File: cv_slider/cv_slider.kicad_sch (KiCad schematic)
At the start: 11 parts, among them J1 I/O connector, U1 HT7550-1, U2 TLV6001UIDBVR

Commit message: Added LCSC part
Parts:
- U2: LCSC (none) -> C544299
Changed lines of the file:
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@@
       (effects (font (size 1.27 1.27)) (justify left) hide)
     )
-    (property "Datasheet" "" (id 3) (at 144.78 99.06 0)
+    (property "Datasheet" "https://www.ti.com/lit/ds/symlink/tlv6001.pdf" (id 3) (at 144.78 99.06 0)
       (effects (font (size 1.27 1.27)) hide)
     )
+    (property "LCSC" "C544299" (id 4) (at 144.78 104.14 0)
+      (effects (font (size 1.524 1.524)) hide)
+    )
     (pin "2")

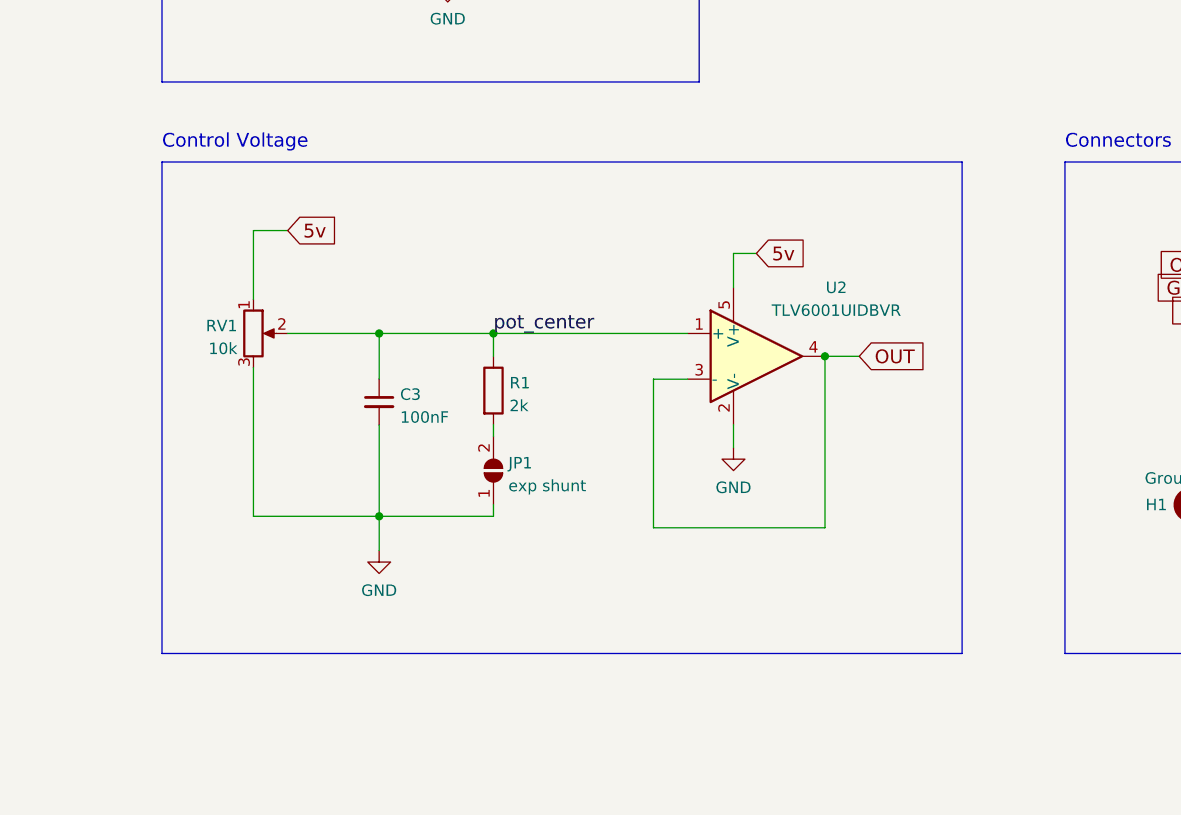
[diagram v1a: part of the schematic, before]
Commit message: Added 1k output resistor
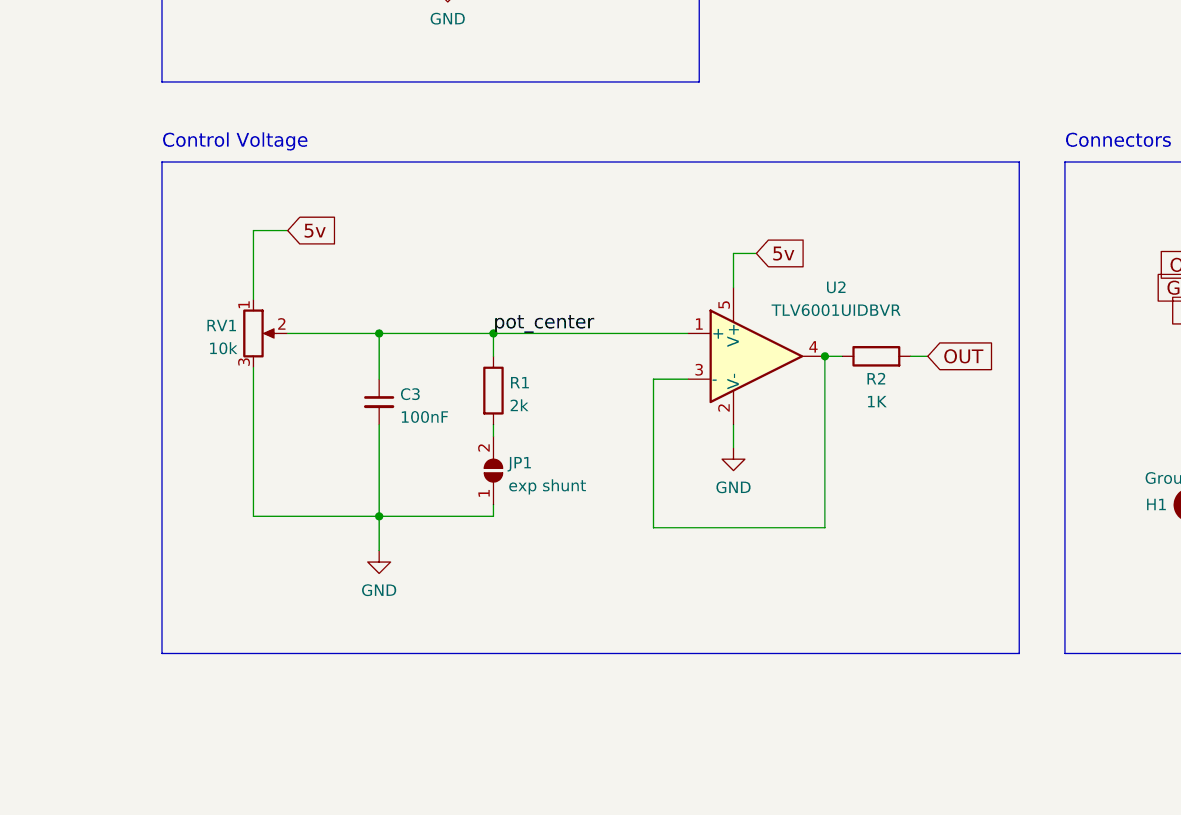
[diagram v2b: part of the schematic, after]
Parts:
- added R2: 1K, Resistor_SMD:R_0402_1005Metric, symbol Device:R
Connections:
- net OUT: now also R2.2; no longer U2.3 (-), U2.4
- new net: R2.1, U2.3 (-), U2.4
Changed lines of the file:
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@@
-    (stroke (width 0) (type default) (color 0 0 0 0))
-  )
-  (wire (pts (xy 152.4 104.14) (xy 156.21 104.14))
     (stroke (width 0) (type default) (color 0 0 0 0))
   )
@@
     (stroke (width 0) (type default) (color 0 0 0 0))
   )
-  (polyline (pts (xy 78.74 82.55) (xy 167.64 82.55))
+  (polyline (pts (xy 78.74 82.55) (xy 173.99 82.55))
     (stroke (width 0) (type default) (color 0 0 0 0))
   )
@@
     (stroke (width 0) (type default) (color 0 0 0 0))
   )
-  (polyline (pts (xy 167.64 82.55) (xy 167.64 137.16))
+  (polyline (pts (xy 173.99 82.55) (xy 173.99 137.16))
+    (stroke (width 0) (type default) (color 0 0 0 0))
+  )
+  (wire (pts (xy 161.925 104.14) (xy 163.83 104.14))
     (stroke (width 0) (type default) (color 0 0 0 0))
   )
@@
     (stroke (width 0) (type default) (color 0 0 0 0))
   )
-  (polyline (pts (xy 167.64 137.16) (xy 78.74 137.16))
+  (polyline (pts (xy 173.99 137.16) (xy 78.74 137.16))
     (stroke (width 0) (type default) (color 0 0 0 0))
   )
@@
   )
   (wire (pts (xy 142.24 96.52) (xy 142.24 92.71))
+    (stroke (width 0) (type default) (color 0 0 0 0))
+  )
+  (wire (pts (xy 152.4 104.14) (xy 154.305 104.14))
     (stroke (width 0) (type default) (color 0 0 0 0))
   )
@@
     )
   )
-  (global_label "OUT" (shape input) (at 156.21 104.14 0) (fields_autoplaced)
+  (global_label "OUT" (shape input) (at 163.83 104.14 0) (fields_autoplaced)
     (effects (font (size 1.524 1.524)) (justify left))
-    (property "Intersheet References" "${INTERSHEET_REFS}" (id 0) (at 163.3532 104.0448 0)
+    (property "Intersheet References" "${INTERSHEET_REFS}" (id 0) (at 170.9732 104.0448 0)
       (effects (font (size 1.524 1.524)) (justify left) hide)
     )
@@
     )
     (pin "1")
+  )
+  (symbol (lib_id "Device:R") (at 158.115 104.14 90) (unit 1)
+    (in_bom yes) (on_board yes)
+    (property "Reference" "R2" (id 0) (at 158.115 106.6831 90))
+    (property "Value" "1K" (id 1) (at 158.115 109.22 90))
+    (property "Footprint" "Resistor_SMD:R_0402_1005Metric" (id 2) (at 158.115 105.918 90)
+      (effects (font (size 1.27 1.27)) hide)
+    )
+    (property "Datasheet" "~" (id 3) (at 158.115 104.14 0)
+      (effects (font (size 1.27 1.27)) hide)
+    )
+    (property "LCSC" "C11702" (id 4) (at 158.115 104.14 0)
+      (effects (font (size 1.524 1.524)) hide)
+    )
+    (pin "1")
+    (pin "2")
   )
   (symbol (lib_id "power:PWR_FLAG") (at 124.46 59.69 180) (unit 1)
@@
       (reference "R1") (unit 1) (value "2k") (footprint "Resistor_SMD:R_0402_1005Metric")
     )
+    (path "/5d8a21c6-2de7-445f-ab12-c2879dbf2517"
+      (reference "R2") (unit 1) (value "1K") (footprint "Resistor_SMD:R_0402_1005Metric")
+    )
     (path "/9763309a-c9ed-492f-a4a9-0b6f407725b0"

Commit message: Fabricating cv-slider prototype
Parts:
- J1: JLCPCB_CORRECTION (none) -> 0;0;90; LCSC (none) -> C5242196
- U1, U2: JLCPCB_CORRECTION (none) -> 0;0;180
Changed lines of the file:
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@@
       (effects (font (size 1.524 1.524)) hide)
+    )
+    (property "JLCPCB_CORRECTION" "0;0;180" (id 5) (at 110.49 48.26 0)
+      (effects (font (size 1.27 1.27)) hide)
     )
     (pin "1")
@@
       (effects (font (size 1.27 1.27)) hide)
     )
+    (property "LCSC" "C5242196" (id 4) (at 201.93 96.52 0)
+      (effects (font (size 1.524 1.524)) hide)
+    )
+    (property "JLCPCB_CORRECTION" "0;0;90" (id 5) (at 201.93 96.52 0)
+      (effects (font (size 1.524 1.524)) hide)
+    )
     (pin "1")
     (pin "2")
@@
       (effects (font (size 1.524 1.524)) hide)
     )
+    (property "JLCPCB_CORRECTION" "0;0;180" (id 5) (at 144.78 104.14 0)
+      (effects (font (size 1.27 1.27)) hide)
+    )
     (pin "2")

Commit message: PCB manufacturing adjustments
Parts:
- removed H1: Ground Pad, cycfi_library:single-pad-2x2-circular, symbol Mechanical:MountingHole_Pad
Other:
- company: Document Number: 2022004 -> Document Number: 2024003
- title: CV Pot Small -> CV Slider
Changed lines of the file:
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@@
   (paper "A4")
   (title_block
-    (title "CV Pot Small")
-    (date "2022-02-24")
-    (rev "v3.0")
-    (company "Document Number: 2022004")
+    (title "CV Slider")
+    (date "2024-10-27")
+    (rev "v1.0")
+    (company "Document Number: 2024003")
   )
   (junction (at 115.57 101.6) (diameter 0) (color 0 0 0 0)
@@
   )
   (polyline (pts (xy 217.17 137.16) (xy 179.07 137.16))
-    (stroke (width 0) (type default) (color 0 0 0 0))
-  )
-  (wire (pts (xy 196.85 120.65) (xy 201.93 120.65))
-    (stroke (width 0) (type default) (color 0 0 0 0))
-  )
-  (wire (pts (xy 201.93 120.65) (xy 201.93 124.46))
     (stroke (width 0) (type default) (color 0 0 0 0))
   )
@@
     (pin "2")
     (pin "3")
-  )
-  (symbol (lib_id "Mechanical:MountingHole_Pad") (at 194.31 120.65 90) (unit 1)
-    (in_bom yes) (on_board yes)
-    (property "Reference" "H1" (id 0) (at 189.23 120.65 90))
-    (property "Value" "Ground Pad" (id 1) (at 193.04 117.7091 90))
-    (property "Footprint" "cycfi_library:single-pad-2x2-circular" (id 2) (at 194.31 120.65 0)
-      (effects (font (size 1.27 1.27)) hide)
-    )
-    (property "Datasheet" "~" (id 3) (at 194.31 120.65 0)
-      (effects (font (size 1.27 1.27)) hide)
-    )
-    (pin "1")
   )
   (symbol (lib_id "power:PWR_FLAG") (at 99.06 44.45 0) (unit 1)
@@
     (pin "4")
   )
-  (symbol (lib_id "power:GND") (at 201.93 124.46 0) (unit 1)
-    (in_bom yes) (on_board yes) (fields_autoplaced)
-    (property "Reference" "#PWR03" (id 0) (at 201.93 130.81 0)
-      (effects (font (size 1.27 1.27)) hide)
-    )
-    (property "Value" "GND" (id 1) (at 201.93 128.9034 0))
-    (property "Footprint" "" (id 2) (at 201.93 124.46 0)
-      (effects (font (size 1.27 1.27)) hide)
-    )
-    (property "Datasheet" "" (id 3) (at 201.93 124.46 0)
-      (effects (font (size 1.27 1.27)) hide)
-    )
-    (pin "1")
-  )
   (sheet_instances
     (path "/" (page "1"))
@@
       (reference "#PWR02") (unit 1) (value "GND") (footprint "")
     )
-    (path "/ff1cc1a1-c8ba-49a8-98aa-0bcf4fbbeed4"
-      (reference "#PWR03") (unit 1) (value "GND") (footprint "")
-    )
     (path "/3e5b385e-4a64-4053-880e-e0031299a98c"
       (reference "#PWR05") (unit 1) (value "GND") (footprint "")
@@
       (reference "D1") (unit 1) (value "1N4148W") (footprint "Diode_SMD:D_SOD-123")
     )
-    (path "/c20c34dc-0c8a-47c9-82f1-fe8a3533aa64"
-      (reference "H1") (unit 1) (value "Ground Pad") (footprint "cycfi_library:single-pad-2x2-circular")
-    )
     (path "/cd61a421-8b7f-4ccf-a635-570d47a12576"

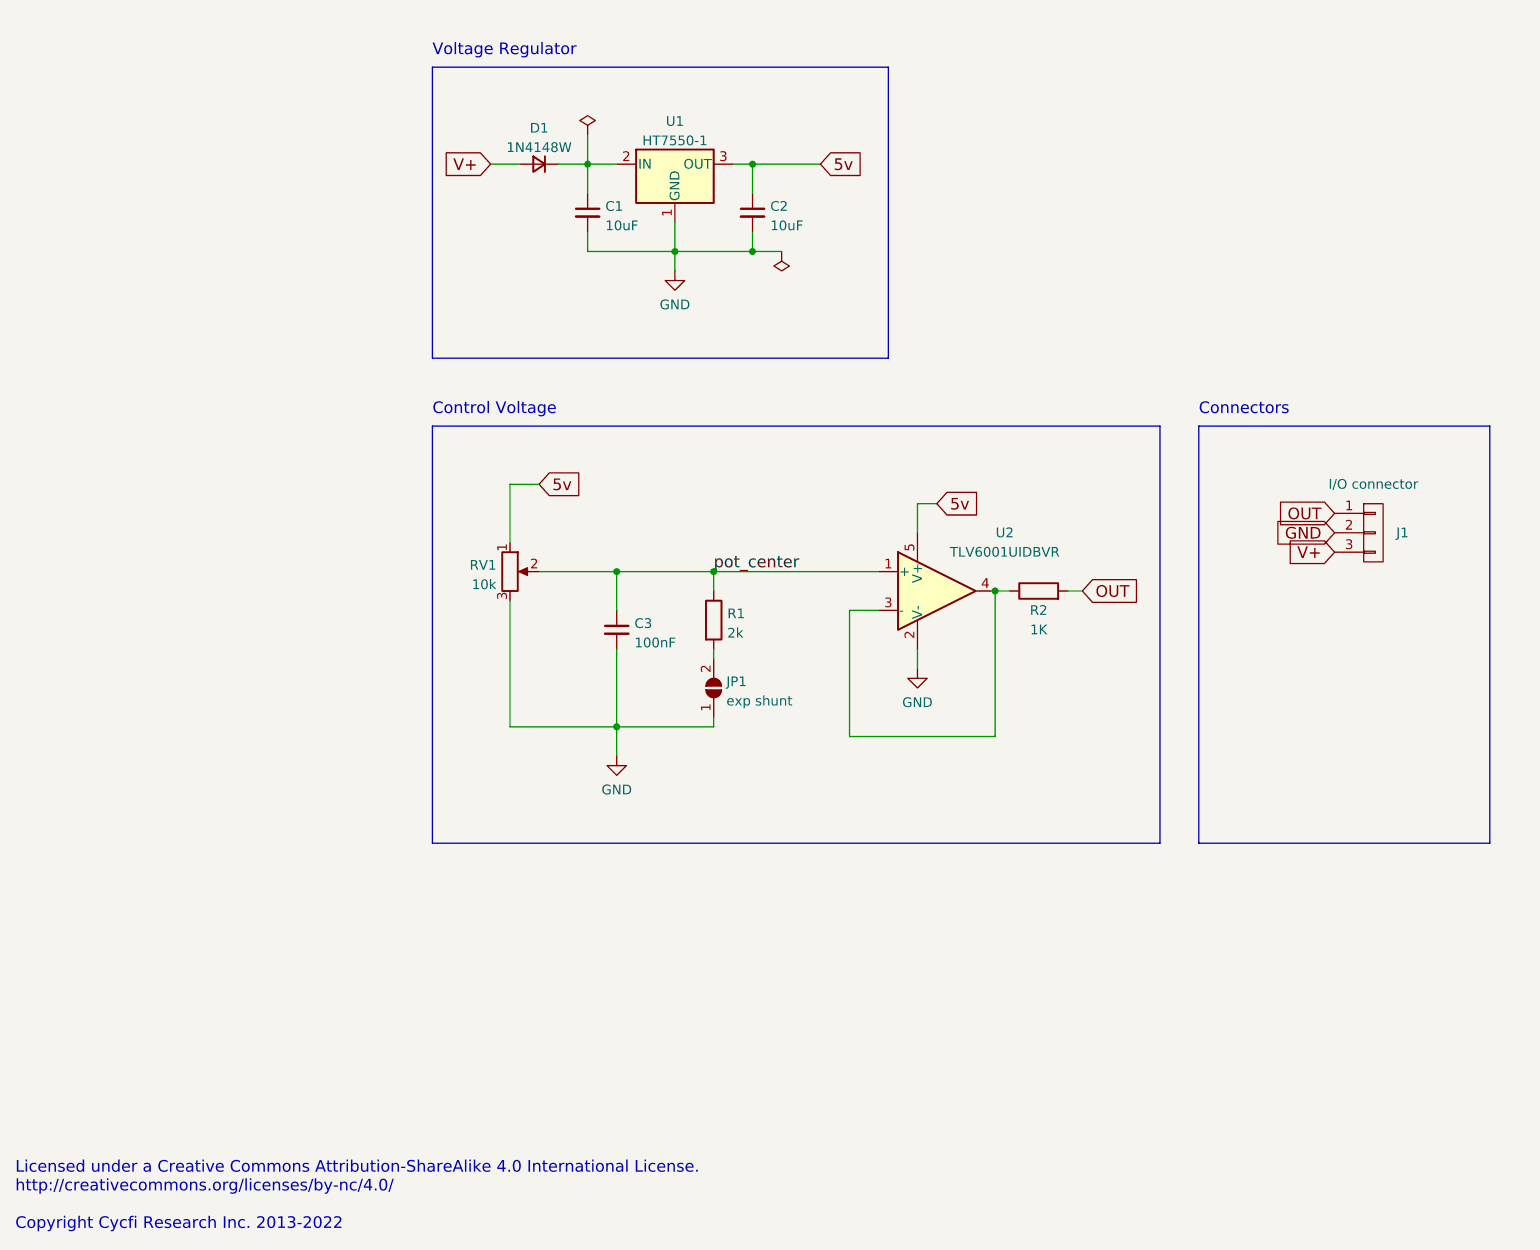
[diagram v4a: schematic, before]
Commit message: Update v1.1 - Added EXP and LOG taper shunts
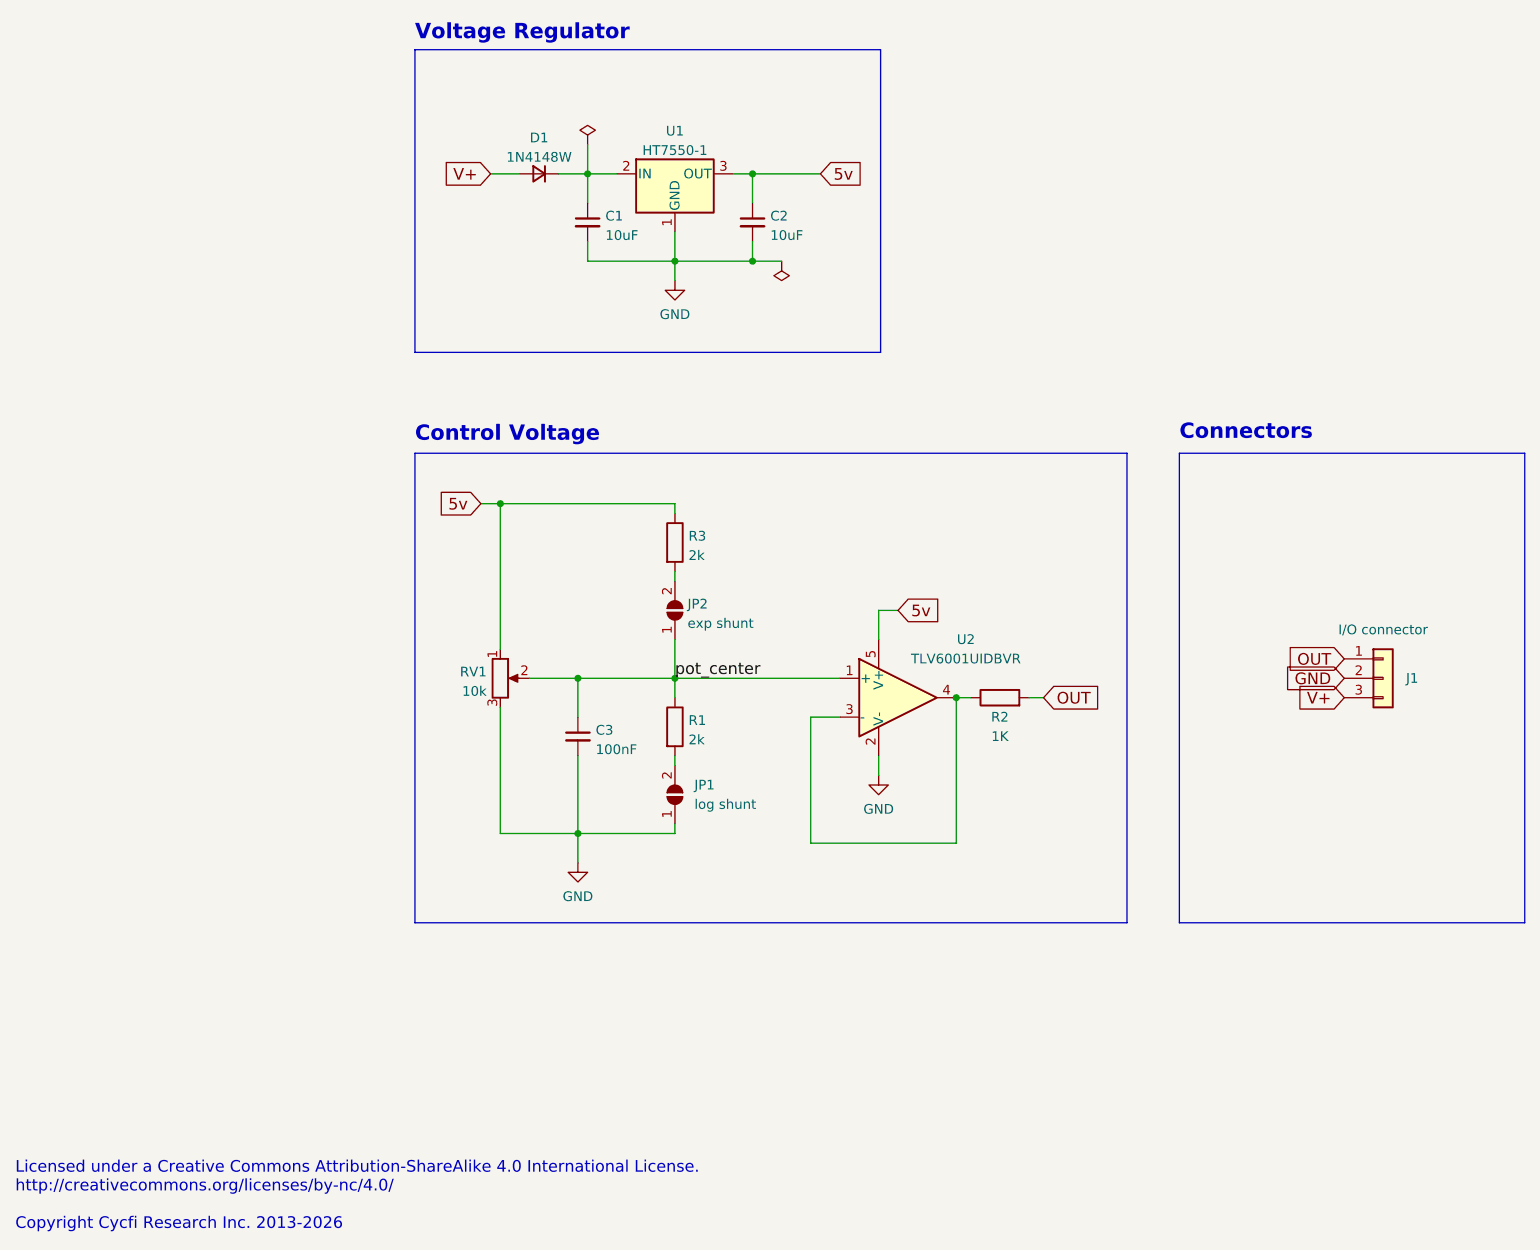
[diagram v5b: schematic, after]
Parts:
- added JP2: exp shunt, Jumper:SolderJumper-2_P1.3mm_Open_TrianglePad1.0x1.5mm, symbol Jumper:SolderJumper_2_Open
- added R3: 2k, Resistor_SMD:R_0402_1005Metric, symbol Device:R
- J1: symbol cycfi_library:conn_1x3 -> Connector_Generic:Conn_01x03
- JP1: value exp shunt -> log shunt
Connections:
- net 5v: now also R3.1
- net pot_center: now also JP2.1 (A)
- new net: JP2.2 (B), R3.2
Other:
- note added: "Licensed under a Creative Commons Attribution-ShareAlike 4.0 International License. http://creativecommons.org/licenses/by-nc/4.0/ Copyright Cycfi Research Inc. 2013-2026"
- note removed: "Licensed under a Creative Commons Attribution-ShareAlike 4.0 International License. http://creativecommons.org/licenses/by-nc/4.0/ Copyright Cycfi Research Inc. 2013-2022"
- moved on the sheet: C1, C2, C3, D1, JP1, R1, R2, RV1, U1, U2
